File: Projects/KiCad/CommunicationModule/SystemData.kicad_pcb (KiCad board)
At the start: 2 copper layers, 110 x 95 mm, 26 parts, among them J1 Conn_01x04_Pin, J2 Conn_01x04_Pin, J3 Micro_SD_Card_Det_Hirose_DM3AT, U1 ABX00012, U2 MCP2562-E-P, U3 LT1584-3.3, U4 TLP222A, U5 MCP2515-I/P, Y1 8MHz

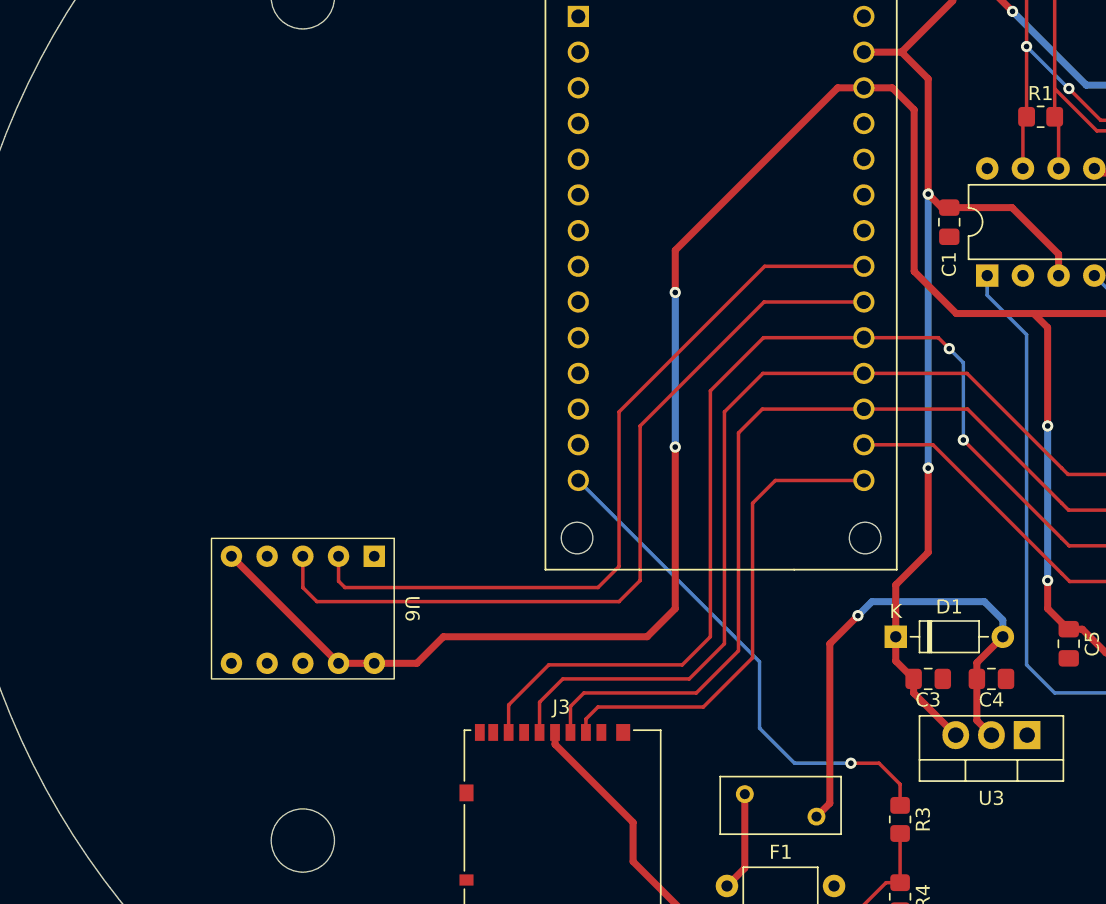
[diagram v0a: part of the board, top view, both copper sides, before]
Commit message: ミッションモジュール, エアデータ通信モジュール, システムデータ通信モジュールのKiCadを追加
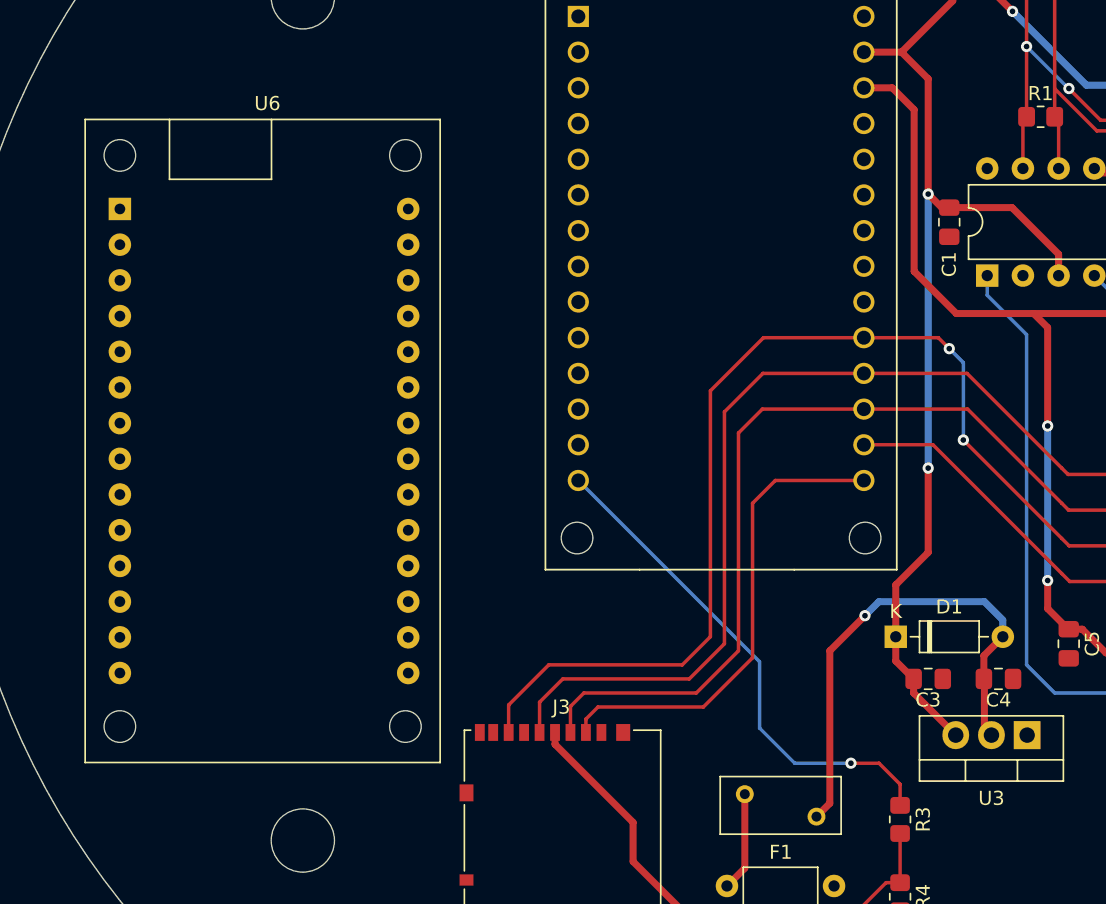
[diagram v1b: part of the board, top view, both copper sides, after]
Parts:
- U6: footprint StrawberryLinux_ADXL375_Module:ADXL375 -> ArduinoMkrGpsShield:Arduino MKR GPS Shield
- moved U6 34.5 mm to (105.5, 90.1), turned to 0 degrees
- moved C4 0.50 mm to (168.0, 123.5)
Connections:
- U6 pad 1: GND -> unconnected-(U6-Pad1)
- U6 pad 10: +3.3V -> unconnected-(U6-Pad10)
- U6 pad 2: I2C_SCL -> unconnected-(U6-Pad2)
- U6 pad 3: I2C_SDA -> unconnected-(U6-Pad3)
- U6 pad 5: +3.3V -> unconnected-(U6-Pad5)
- U6 pad 8: GND -> unconnected-(U6-Pad8)
- U6 pad 9: +3.3V -> unconnected-(U6-Pad9)
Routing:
- net +3.3V: track 159.2 -> 79.2 mm, vias 4 -> 2
- net I2C_SDA: track 57.8 -> 0.00 mm
- net I2C_SCL: track 55.3 -> 0.00 mm
- net Net-(D1-A): track 36.2 -> 35.5 mm

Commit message: 全モジュールのkicadを一通り作った
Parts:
- removed the C3 at (163.0, 123.5)
- removed the C4 at (168.0, 123.5)
- removed F1: Polyfuse, Fuse:Fuse_BelFuse_0ZRE0005FF_L8.3mm_W3.8mm
- removed J3: Micro_SD_Card_Det_Hirose_DM3AT, Connector_Card:microSD_HC_Hirose_DM3AT-SF-PEJM5
- removed the U3 at (170.0, 127.5)
- removed the U4 at (156.3, 140.8)
- added D2: LED, LED_SMD:LED_1206_3216Metric_Pad1.42x1.75mm_HandSolder, F.Cu at (195.5, 109.5)
- added D3: LED, LED_SMD:LED_1206_3216Metric_Pad1.42x1.75mm_HandSolder, F.Cu at (195.7, 116.0)
- added D4: LED, LED_SMD:LED_1206_3216Metric_Pad1.42x1.75mm_HandSolder, F.Cu at (158.5, 132.5)
- added D5: LED, LED_SMD:LED_1206_3216Metric_Pad1.42x1.75mm_HandSolder, F.Cu at (152.0, 132.5)
- added D6: LED, LED_SMD:LED_1206_3216Metric_Pad1.42x1.75mm_HandSolder, F.Cu at (130.0, 126.0)
- added R2: 10kΩ, Resistor_SMD:R_0805_2012Metric_Pad1.20x1.40mm_HandSolder, F.Cu at (172.5, 119.5)
- added R5: 100Ω, Resistor_SMD:R_0805_2012Metric_Pad1.20x1.40mm_HandSolder, F.Cu at (190.0, 116.0)
- added R6: 100Ω, Resistor_SMD:R_0805_2012Metric_Pad1.20x1.40mm_HandSolder, F.Cu at (158.5, 126.0)
- added R7: 100Ω, Resistor_SMD:R_0805_2012Metric_Pad1.20x1.40mm_HandSolder, F.Cu at (152.0, 126.0)
- added R8: 100Ω, Resistor_SMD:R_0805_2012Metric_Pad1.20x1.40mm_HandSolder, F.Cu at (130.0, 120.0)
- added SW1: SW_Push, Button_Switch_THT:SW_PUSH_6mm, F.Cu at (143.5, 131.5)
- D1: value 1N4148 -> LED; footprint Diode_THT:D_DO-35_SOD27_P7.62mm_Horizontal -> LED_SMD:LED_1206_3216Metric_Pad1.42x1.75mm_HandSolder
- R3: value 120Ω -> 2kΩ
- R4: value 120Ω -> 100Ω
- moved R3 62.6 mm to (187.0, 76.5), turned to 0 degrees
- moved D1 54.3 mm to (187.0, 73.0)
- moved R4 41.4 mm to (190.0, 109.5), turned to 0 degrees
- moved U3 2.49 mm to (103.0, 89.8)
- moved C3 1.12 mm to (172.5, 122.0), turned to 180 degrees
- renumbered C5 to C3, C6 to C4, C7 to C5, U6 to U3, U5 to U4
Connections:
- D1 pad 1: +5V -> GND
- R3 pad 1: MEMORY_POWER_CONTROL -> +5V
- R3 pad 2: Net-(R3-Pad2) -> Net-(D1-A)
- R4 pad 1: Net-(R3-Pad2) -> CAN_RECEIVE_STATUS
- R4 pad 2: GND -> Net-(D2-A)
- U1 pad 10: unconnected-(U1-PA23_TC4-W1/1-Pad10) -> CAN_RECEIVE_STATUS
- U1 pad 11: unconnected-(U1-PA10_TCC0-W2/~2-Pad11) -> CAN_SEND_STATUS
- U1 pad 12: unconnected-(U1-PA11_TCC0-W3/~3-Pad12) -> LORA_RECEIVE_STATUS
- U1 pad 13: unconnected-(U1-PB10_TCC0-W4/~4-Pad13) -> LORA_SEND_STATUS
- U1 pad 14: MEMORY_POWER_CONTROL -> GNSS_STATUS
- U1 pad 15: SPI_CS_SD -> unconnected-(U1-PA20_TCC0-W6-Pad15)
- U1 pad 20: I2C_SDA -> unconnected-(U1-PA08_S0_I2C_SDA-Pad20)
- U1 pad 21: I2C_SCL -> unconnected-(U1-PA09_S0_I2C_SCL-Pad21)
- U1 pad 9: unconnected-(U1-PA22_TC4-W0/0-Pad9) -> DEBUG_MODE
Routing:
- net CAN_RECEIVE_STATUS: track 0.00 -> 76.3 mm
- net CAN_SEND_STATUS: track 0.00 -> 69.6 mm
- net SPI_MISO: track 75.9 -> 27.6 mm
- net SPI_SCLK: track 65.8 -> 21.2 mm
- net DEBUG_MODE: track 0.00 -> 41.8 mm
- net SPI_MOSI: track 61.8 -> 21.2 mm
- net +5V: track 106.8 -> 70.7 mm, vias 3 -> 1
- net MEMORY_POWER_CONTROL: track 36.1 -> 0.00 mm, vias 1 -> 0
- net SPI_CS_SD: track 34.2 -> 0.00 mm
- net Net-(D1-A): track 35.5 -> 3.70 mm, vias 1 -> 0
- net LORA_RECEIVE_STATUS: track 0.00 -> 31.0 mm
- net LORA_SEND_STATUS: track 0.00 -> 26.7 mm
- net MEMORY_POWER: track 19.9 -> 0.00 mm
- net GNSS_STATUS: track 0.00 -> 13.8 mm
- net Net-(R3-Pad2): track 9.35 -> 0.00 mm
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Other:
- board text added: "Boot Selection"
- board text added: "CAN"
- board text added: "CAN-BUS TERMINATION RESISTOR (OPTIONAL)"
- board text added: "DEBUG"
- board text added: "GNSS Status"
- board text added: "LORA"
- board text added: "POWER"
- board text added: "RECEIVE"
- board text added: "SEND"

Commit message: 一通り部品を選定
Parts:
- C4, C5: footprint Capacitor_SMD:C_0805_2012Metric_Pad1.18x1.45mm_HandSolder -> Capacitor_SMD:C_0603_1608Metric_Pad1.08x0.95mm_HandSolder
- D1: value LED -> RED; footprint LED_SMD:LED_1206_3216Metric_Pad1.42x1.75mm_HandSolder -> LED_SMD:LED_0603_1608Metric_Pad1.05x0.95mm_HandSolder
- D2, D3, D4, D5: value LED -> ORANGE; footprint LED_SMD:LED_1206_3216Metric_Pad1.42x1.75mm_HandSolder -> LED_SMD:LED_0603_1608Metric_Pad1.05x0.95mm_HandSolder
- D6: value LED -> GREEN; footprint LED_SMD:LED_1206_3216Metric_Pad1.42x1.75mm_HandSolder -> LED_SMD:LED_0603_1608Metric_Pad1.05x0.95mm_HandSolder
- R1: value 120R1/4W -> 120Ω; footprint Resistor_SMD:R_0805_2012Metric_Pad1.20x1.40mm_HandSolder -> Resistor_SMD:R_0603_1608Metric_Pad0.98x0.95mm_HandSolder
- R2, R4, R5, R6, R7: footprint Resistor_SMD:R_0805_2012Metric_Pad1.20x1.40mm_HandSolder -> Resistor_SMD:R_0603_1608Metric_Pad0.98x0.95mm_HandSolder
- R3: value 2kΩ -> 620Ω; footprint Resistor_SMD:R_0805_2012Metric_Pad1.20x1.40mm_HandSolder -> Resistor_SMD:R_0603_1608Metric_Pad0.98x0.95mm_HandSolder
- R8: value 100Ω -> 300Ω; footprint Resistor_SMD:R_0805_2012Metric_Pad1.20x1.40mm_HandSolder -> Resistor_SMD:R_0603_1608Metric_Pad0.98x0.95mm_HandSolder
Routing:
- net Net-(D5-A): track 4.01 -> 4.62 mm
- net Net-(D4-A): track 4.01 -> 4.62 mm
- net Net-(D3-A): track 3.17 -> 3.78 mm
- net Net-(D2-A): track 3.01 -> 3.62 mm
- net Net-(D6-A): track 3.51 -> 4.12 mm

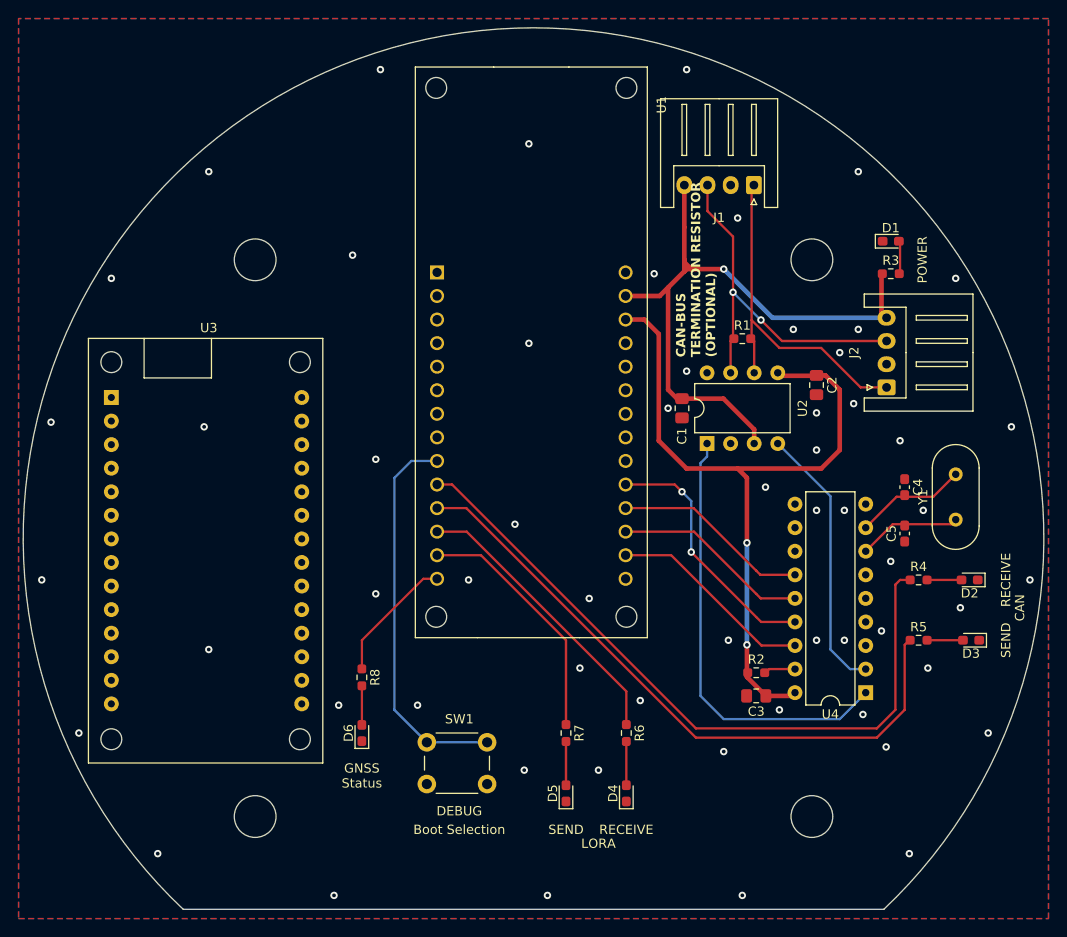
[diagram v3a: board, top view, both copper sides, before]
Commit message: コネクタを再配置, 基板上で12V->5Vをするように変更
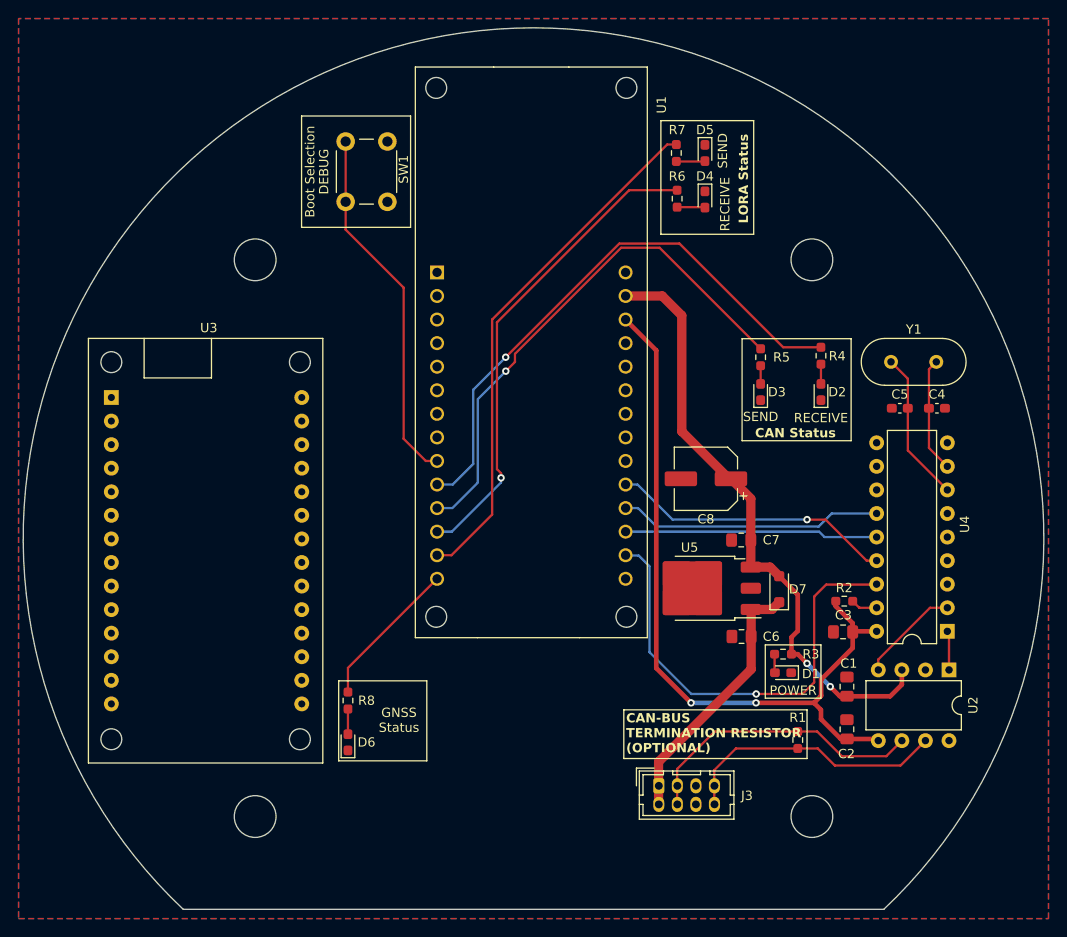
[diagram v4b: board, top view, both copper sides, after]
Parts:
- removed J1, J2: Conn_01x04_Pin, Connector_JST:JST_XH_S4B-XH-A_1x04_P2.50mm_Horizontal
- added C6: 0.33μF, Capacitor_SMD:C_0805_2012Metric_Pad1.18x1.45mm_HandSolder, F.Cu at (170.9, 115.6)
- added C7: 0.1μF, Capacitor_SMD:C_0805_2012Metric_Pad1.18x1.45mm_HandSolder, F.Cu at (170.9, 105.2)
- added C8: 100μF, Capacitor_SMD:CP_Elec_6.3x7.7, F.Cu at (167.1, 98.6)
- added D7: 1N4007, Diode_SMD:D_SOD-123F, F.Cu at (175.0, 110.5)
- added J3: Conn_01x08, Connector_Hirose:Hirose_DF11-8DP-2DSA_2x04_P2.00mm_Vertical, F.Cu at (162.0, 131.7)
- added U5: NJM7805SDL1, Package_TO_SOT_SMD:TO-252-3_TabPin2, F.Cu at (166.9, 110.4)
- moved D5 70.6 mm to (167.0, 63.5), turned to -90 degrees
- moved SW1 70.1 mm to (132.8, 62.2), turned to -90 degrees
- moved D4 64.6 mm to (167.0, 68.5), turned to -90 degrees
- moved R7 63.6 mm to (163.9, 63.5)
- moved R6 57.8 mm to (164.0, 68.4)
- moved D1 47.9 mm to (175.4, 119.5), turned to 180 degrees
- moved R1 43.7 mm to (177.0, 126.8), turned to 90 degrees
- moved R3 42.6 mm to (175.4, 117.5), turned to 180 degrees
- moved C2 37.2 mm to (182.3, 125.6), turned to 90 degrees
- moved U2 35.7 mm to (193.3, 119.2), turned to -90 degrees
- moved D3 35.1 mm to (173.0, 89.3), turned to 90 degrees
- moved R5 34.9 mm to (173.0, 85.5), turned to -90 degrees
- moved C1 34.9 mm to (182.3, 121.0), turned to 90 degrees
- moved R4 26.4 mm to (179.5, 85.3), turned to -90 degrees
- moved D2 25.8 mm to (179.5, 89.3), turned to 90 degrees
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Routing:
- net CAN_TX: track 47.5 -> 3.98 mm
- net LORA_SEND_STATUS: track 26.7 -> 56.4 mm
- net +12V: track 0.00 -> 28.5 mm
- net SPI_CS_MCP: track 22.3 -> 49.0 mm, vias 0 -> 1
- net LORA_RECEIVE_STATUS: track 31.0 -> 51.8 mm, vias 0 -> 1
- net CAN_RX: track 29.2 -> 10.9 mm
- net CAN_RECEIVE_STATUS: track 76.3 -> 61.4 mm, vias 0 -> 1
- net CAN_SEND_STATUS: track 69.6 -> 56.8 mm, vias 0 -> 1
- net CAN_H: track 40.2 -> 29.3 mm, vias 2 -> 0
- net SPI_SCLK: track 21.2 -> 28.5 mm
- net CAN_L: track 38.0 -> 31.5 mm
- net SPI_MOSI: track 21.2 -> 27.3 mm
- net OSC2: track 11.1 -> 16.3 mm
- net +5V: track 70.7 -> 65.9 mm, vias 1 -> 2
- net SPI_MISO: track 27.6 -> 30.5 mm, vias 2 -> 1
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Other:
- board text added: "CAN Status"
- board text added: "LORA Status"
- board text removed: "CAN"
- board text removed: "LORA"

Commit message: 基板設計の都市伝説をいろいろ適応
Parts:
- REF** (x4): value MountingHole_4.5mm -> MountingHole_4.5mm_Pad_Via; footprint MountingHole:MountingHole_4.5mm -> MountingHole:MountingHole_4.5mm_Pad_Via
- moved R1 17.1 mm to (193.9, 129.0), turned to 0 degrees
- renumbered C4 to C1, C3 to C2, C6 to C3, C2 to C4, C1 to C5, C8 to C6, C5 to C8, D7 to D2, D2 to D4, D4 to D5, D5 to D6, D6 to D7, J3 to J1, R3 to R2, R2 to R3, R5 to R4, R4 to R5, U2 to U1, U4 to U2, U5 to U3, U1 to U4, U3 to U5
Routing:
- net CAN_L: track 31.5 -> 43.5 mm
- net CAN_H: track 29.3 -> 39.8 mm
- net +3.3V: track 82.4 -> 84.9 mm, vias 2 -> 4
- net +5V: track 65.9 -> 67.9 mm, vias 2 -> 4
- net LORA_SEND_STATUS: track 56.4 -> 55.5 mm
- net GND: vias 0 -> 158
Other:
- outline, holes or cut-outs redrawn
- board text added: "CAN-BUS Termination Resistor"
- board text removed: "CAN-BUS TERMINATION RESISTOR (OPTIONAL)"

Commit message: 裏面にQRコードと署名を追加
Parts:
- added G***: LOGO, LOGO, B.Cu at (146.0, 74.0)
- added G***: LOGO, LOGO, B.Cu at (148.0, 63.5)
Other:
- board text added: "Communication Module System Data Build 1"
- board text added: "Designed by Y.Iwai 2023"
- board text added: "Tokai Student Rocket Poject H-58 Avionics"

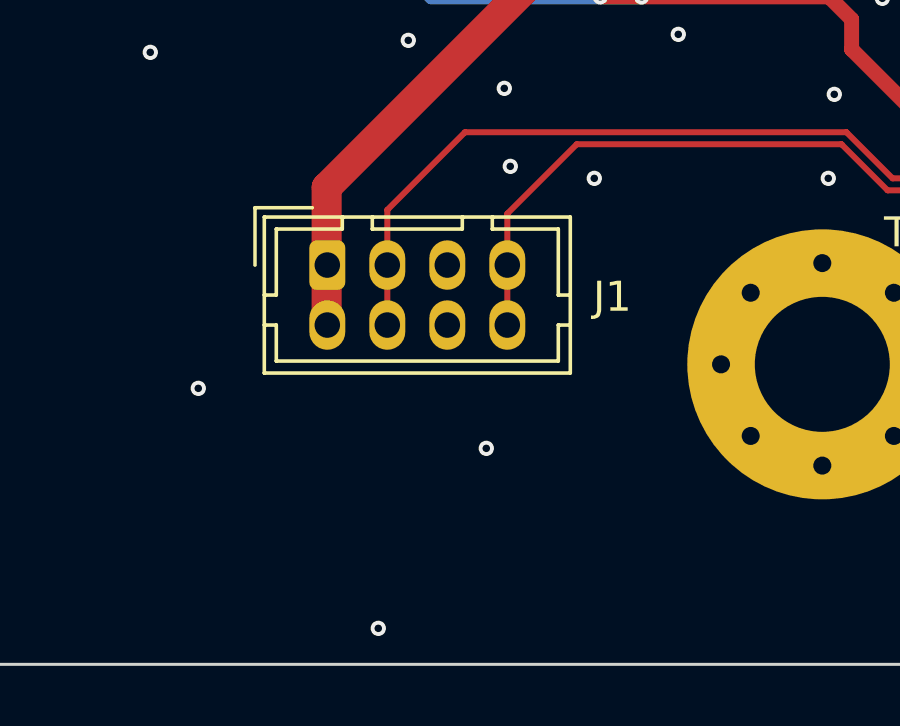
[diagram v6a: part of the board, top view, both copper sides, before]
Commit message: コネクタ類の3Dモデルを追加
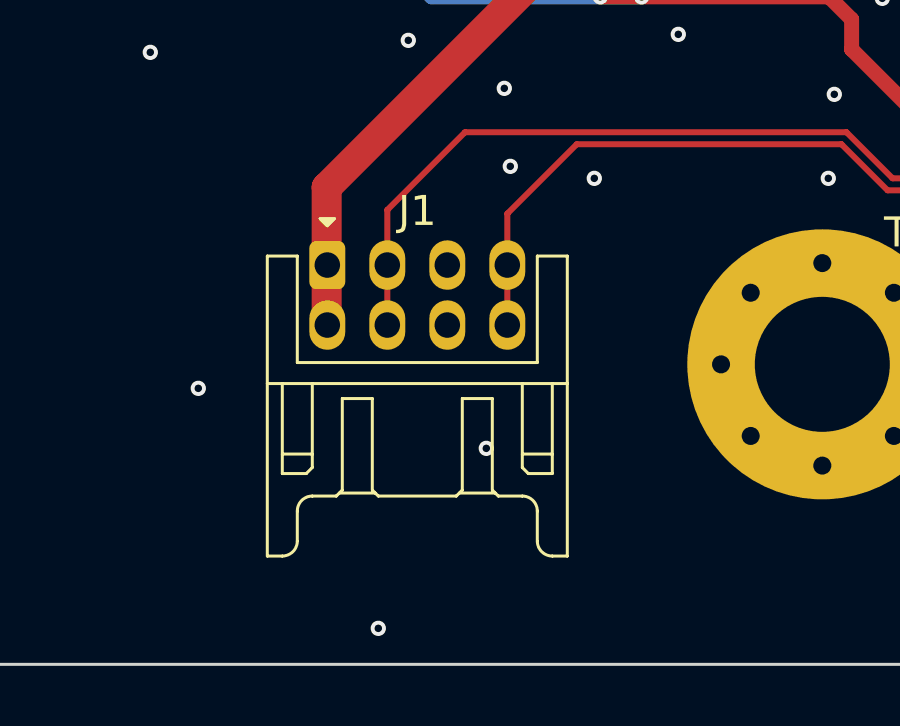
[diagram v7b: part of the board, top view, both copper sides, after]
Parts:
- J1: footprint Connector_Hirose:Hirose_DF11-8DP-2DSA_2x04_P2.00mm_Vertical -> Hirose_Connector:Hirose_DF11B-8DP-2DS
